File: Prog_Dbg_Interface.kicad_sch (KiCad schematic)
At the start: 39 parts, among them J2 GCT_USB4105-GF-A, U1 LFE5U-25F-6BG256C, U5 TPD2EUSB30A, U6 FT231XQ, U7 W25Q128JVS, Y1 OT322550MJBA4SL

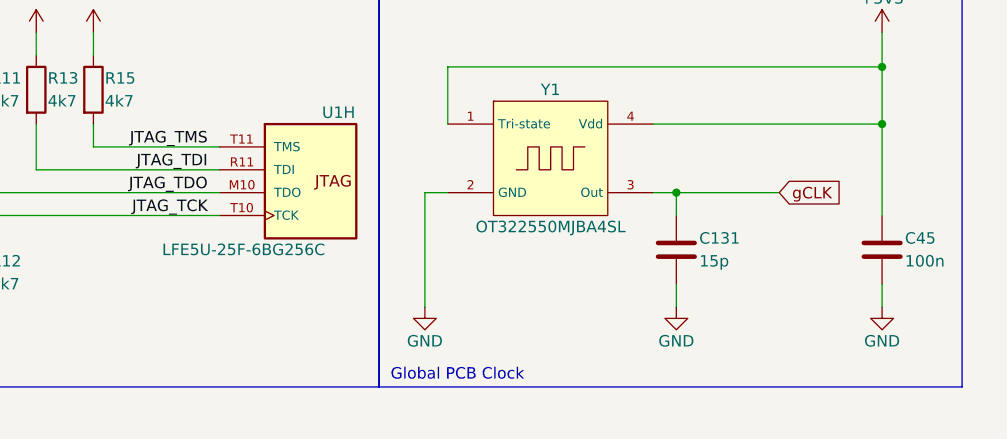
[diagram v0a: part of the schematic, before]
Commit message: Document A bit and add more silkscreen
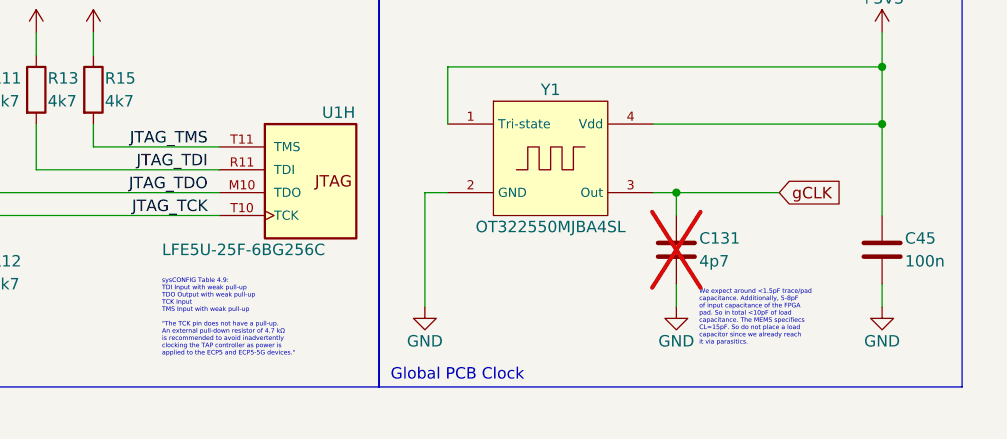
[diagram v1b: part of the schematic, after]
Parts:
- C131: value 15p -> 4p7; now not fitted
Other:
- note added: "We expect around <1.5pF trace/pad capacitance. Additionally, 5-8pF of input capacitance of the FPGA pad. So in total <10pF of load capacitance. The MEMS specifiecs CL=15pF. So do not place a load capacitor since we already reach it via parasitics."
- note added: "sysCONFIG Table 4.9: TDI Input with weak pull-up TDO Output with weak pull-up TCK Input TMS Input with weak pull-up "The TCK pin does not have a pull-up. An external pull-down resistor of 4.7 kΩ is recommended to avoid inadvertently clocking the TAP controller as power is applied to the ECP5 and ECP5-5G devices.""
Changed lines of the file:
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@@
+		)
+	)
+	(text "We expect around <1.5pF trace/pad\ncapacitance. Additionally, 5-8pF\nof input capacitance of the FPGA\npad. So in total <10pF of load\ncapacitance. The MEMS specifiecs\nCL=15pF. So do not place a load\ncapacitor since we already reach\nit via parasitics."
+		(exclude_from_sim no)
+		(at 97.79 140.97 0)
+		(effects
+			(font
+				(size 0.5 0.5)
+			)
+			(justify left)
 		)
 	)
@@
 		(exclude_from_sim no)
 		(at 240.03 82.55 0)
+		(effects
+			(font
+				(size 0.5 0.5)
+			)
+			(justify left)
+		)
+	)
+	(text "sysCONFIG Table 4.9:\nTDI Input with weak pull-up\nTDO Output with weak pull-up\nTCK Input\nTMS Input with weak pull-up\n\n\"The TCK pin does not have a pull-up.\nAn external pull-down resistor of 4.7 kΩ\nis recommended to avoid inadvertently\nclocking the TAP controller as power is\napplied to the ECP5 and ECP5-5G devices.\""
+		(exclude_from_sim no)
+		(at 38.1 140.97 0)
 		(effects
 			(font
@@
 		(in_bom yes)
 		(on_board yes)
-		(dnp no)
+		(dnp yes)
 		(property "Reference" "C131"
 			(at 97.79 132.0799 0)
@@
 			)
 		)
-		(property "Value" "15p"
+		(property "Value" "4p7"
 			(at 97.79 134.6199 0)
 			(effects
